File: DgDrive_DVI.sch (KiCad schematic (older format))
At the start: 26 parts, among them J1 Bias-T, J2 DVI-I, J3 Ld+, J4 Ld-, J5 Pz+, J6 Pz-, J7 Piezo_In, K1 G6AU, Q1 MMBT3904, Q2 2N4401

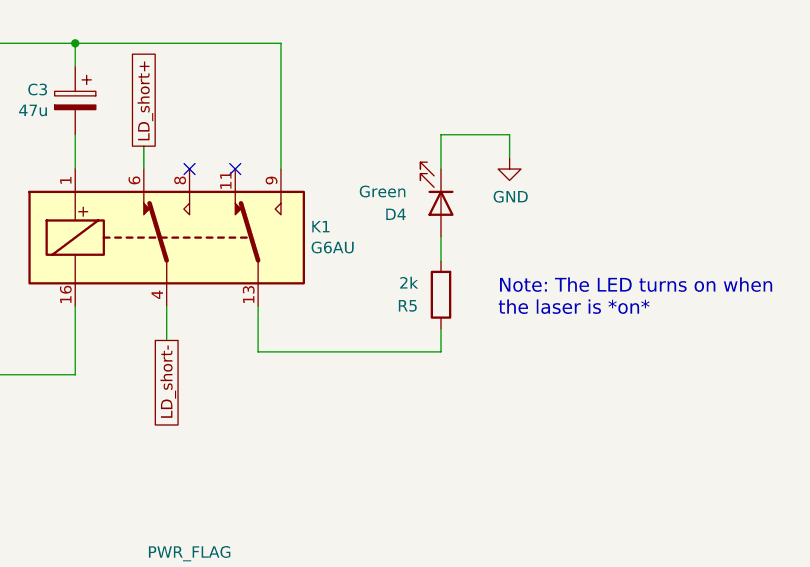
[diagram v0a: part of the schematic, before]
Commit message: Ld-: SMD Pad for shield
Fix footprints and replace Ld- THT with SMD pad
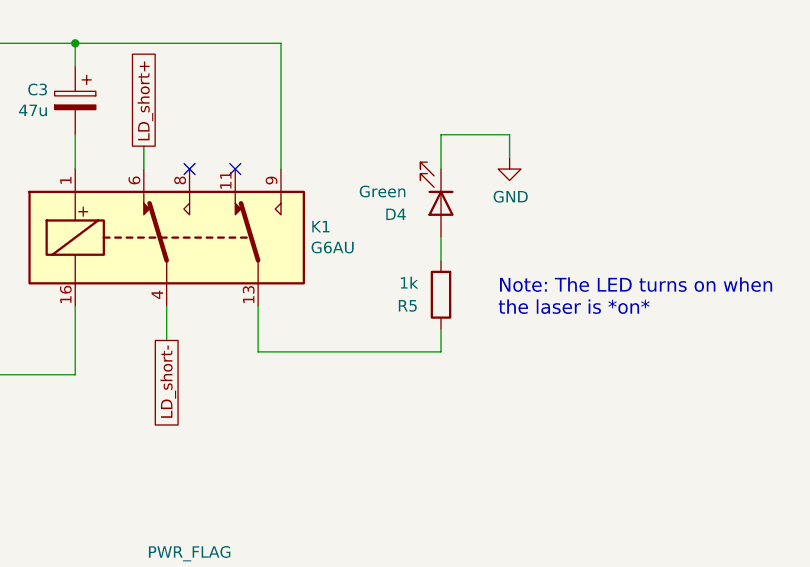
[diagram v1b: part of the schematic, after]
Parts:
- C3: footprint Capacitors_THT:CP_Radial_D5.0mm_P2.00mm -> Capacitor_THT:CP_Radial_D5.0mm_P2.00mm
- J3, J5, J6: footprint Wire_Pads:SolderWirePad_single_1mmDrill -> Connector_Wire:SolderWirePad_1x01_Drill1mm
- J4: footprint Wire_Pads:SolderWirePad_single_1mmDrill -> TestPoint:TestPoint_Keystone_5019_Minature
- R5: value 2k -> 1k; footprint Resistors_SMD:R_0603 -> Resistor_SMD:R_0603_1608Metric
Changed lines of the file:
@@
 Sheet 1 1
 Title "Laser Backplane Diode DVI"
-Date "2020-10-15"
-Rev "1.3"
+Date "2021-03-04"
+Rev "1.3.1"
 Comp "APQ"
 Comment1 "Tilman Preuschoff & Patrick Baus"
@@
 AR Path="/5BC1B30D" Ref="R5"  Part="1"
 F 0 "R5" H 6600 2100 50  0000 L CNN
-F 1 "2k" H 6600 2000 50  0000 L CNN
-F 2 "Resistors_SMD:R_0603" V 6430 2050 50  0001 C CNN
+F 1 "1k" H 6600 2000 50  0000 L CNN
+F 2 "Resistor_SMD:R_0603_1608Metric" V 6430 2050 50  0001 C CNN
 F 3 "~" H 6500 2050 50  0001 C CNN
 	1    6500 2050
@@
 F 0 "C3" H 5018 1246 50  0000 L CNN
 F 1 "47u" H 5018 1155 50  0000 L CNN
-F 2 "Capacitors_THT:CP_Radial_D5.0mm_P2.00mm" H 4938 1050 50  0001 C CNN
+F 2 "Capacitor_THT:CP_Radial_D5.0mm_P2.00mm" H 4938 1050 50  0001 C CNN
 F 3 "" H 4900 1200 50  0001 C CNN
 F 4 "Nichicon" H 4900 1200 60  0001 C CNN "MFN"
@@
 F 0 "J5" H 7568 4075 50  0000 C CNN
 F 1 "Pz+" H 7568 4166 50  0000 C CNN
-F 2 "Wire_Pads:SolderWirePad_single_1mmDrill" H 7650 4300 50  0001 C CNN
+F 2 "Connector_Wire:SolderWirePad_1x01_Drill1mm" H 7650 4300 50  0001 C CNN
 F 3 "~" H 7650 4300 50  0001 C CNN
 	1    7650 4300
@@
 F 0 "J6" H 7568 4425 50  0000 C CNN
 F 1 "Pz-" H 7568 4516 50  0000 C CNN
-F 2 "Wire_Pads:SolderWirePad_single_1mmDrill" H 7650 4650 50  0001 C CNN
+F 2 "Connector_Wire:SolderWirePad_1x01_Drill1mm" H 7650 4650 50  0001 C CNN
 F 3 "~" H 7650 4650 50  0001 C CNN
 	1    7650 4650
@@
 F 0 "J3" H 6930 5542 50  0000 L CNN
 F 1 "Ld+" H 6930 5451 50  0000 L CNN
-F 2 "Wire_Pads:SolderWirePad_single_1mmDrill" H 6850 5500 50  0001 C CNN
+F 2 "Connector_Wire:SolderWirePad_1x01_Drill1mm" H 6850 5500 50  0001 C CNN
 F 3 "~" H 6850 5500 50  0001 C CNN
 	1    6850 5500
@@
 F 0 "J4" H 6930 6142 50  0000 L CNN
 F 1 "Ld-" H 6930 6051 50  0000 L CNN
-F 2 "Wire_Pads:SolderWirePad_single_1mmDrill" H 6850 6100 50  0001 C CNN
+F 2 "TestPoint:TestPoint_Keystone_5019_Minature" H 6850 6100 50  0001 C CNN
 F 3 "~" H 6850 6100 50  0001 C CNN
 	1    6850 6100

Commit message: Incomplete: Add current source
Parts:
- removed C2: 3.3n (C0G), Capacitor_SMD:C_1206_3216Metric, symbol Device:C_Small
- removed R4: 49.9, Resistor_SMD:R_1210_3225Metric, symbol Device:R_Small
- removed TR1: SWB1010, Package_DIP:DIP-6_W7.62mm, symbol Transformer:ADT1-1
- added C? (x2): 10n, Capacitor_SMD:C_0603_1608Metric, symbol Device:C_Small
- added FB? (x2): BLM18KG102SZ1D, Inductor_SMD:L_0603_1608Metric, symbol Device:Ferrite_Bead_Small
- added L? (x2): 3.3u, custom:Coilcraft_XGL3530, symbol Device:L_Small
- added U?: LT1761-5, Package_TO_SOT_SMD:TSOT-23-5, symbol Regulator_Linear:LT1761-5
- J1: value Bias-T -> Curr. Mod.
- R1: value 5.6 / 750 mW -> 49.9; footprint Resistor_SMD:R_2512_6332Metric -> Resistor_SMD:R_0603_1608Metric; MFN Panasonic -> (none); MFP ERJ-1TRQF5R6U -> (none)
- R6: value 5.6 / 750 mW -> 49.9; footprint Resistor_SMD:R_2512_6332Metric -> Resistor_SMD:R_0603_1608Metric
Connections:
- net labels added: +12V, -12V, Curr_Mod
- net labels removed: Relay+
- wire segments 89 -> 100
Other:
- moved on the sheet: J1, J3, J4, J5, J6, J7, Q2, R1, R2, R6, R7, R8

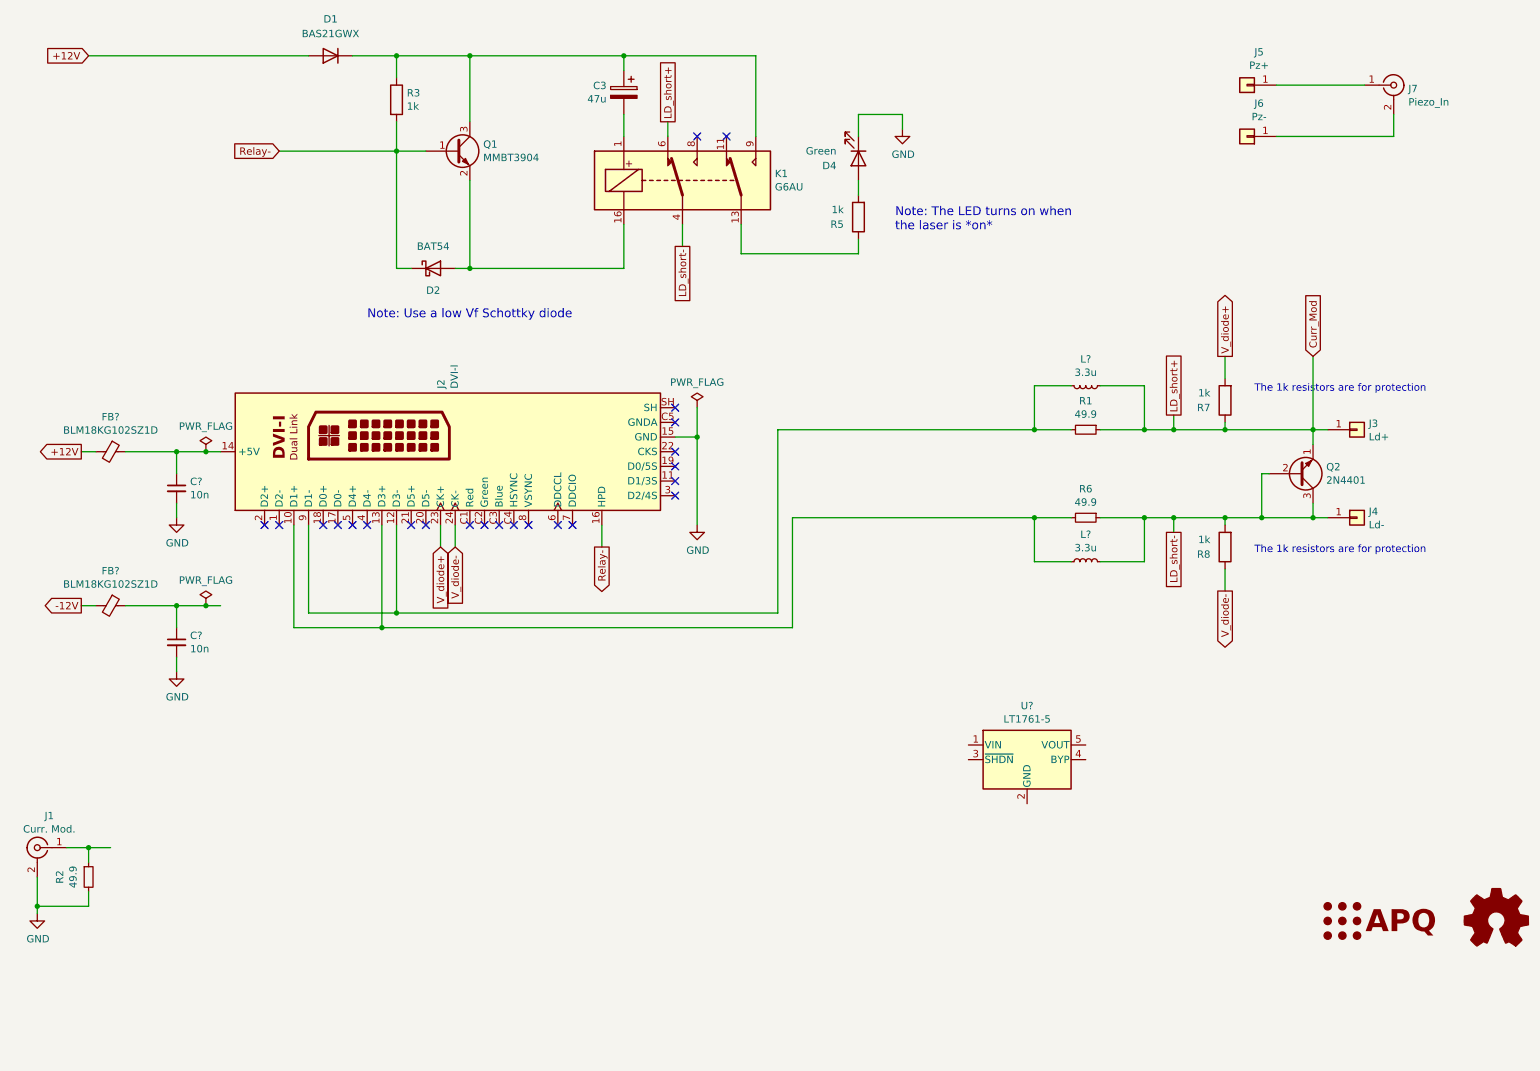
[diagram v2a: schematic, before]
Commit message: Add current source
Replace Bias-T with Howland current source. The current source requires additional negative supply (Pin7).

Replace large resistors with inductors+49.9-resistors.
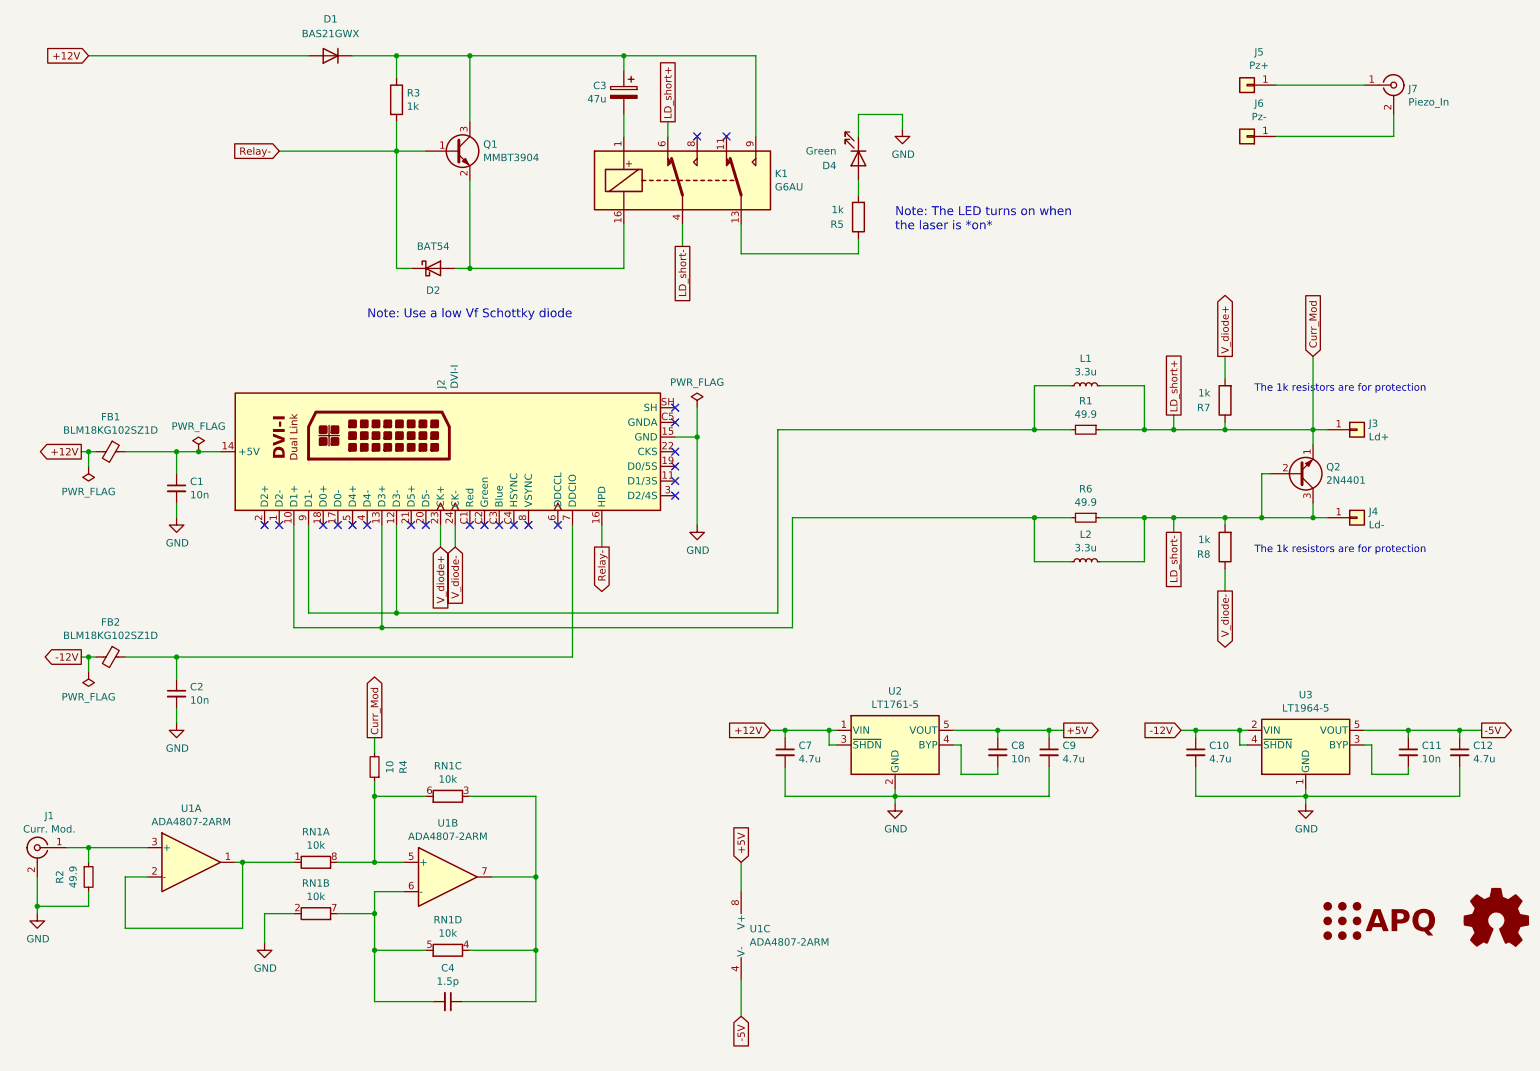
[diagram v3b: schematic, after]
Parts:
- added C10, C12, C7, C9: 4.7u, Capacitor_SMD:C_0805_2012Metric, symbol Device:C_Small
- added C11, C8: 10n, Capacitor_SMD:C_0603_1608Metric, symbol Device:C_Small
- added C4: 1.5p, Capacitor_SMD:C_0603_1608Metric, symbol Device:C_Small
- added R4: 10, Resistor_SMD:R_0603_1608Metric, symbol Device:R_Small
- added RN1: 10k, custom:MSOP-8_3x3mm_P0.65mm_mod, symbol Device:R_Pack04_Split
- added U1: ADA4807-2ARM, custom:MSOP-8_3x3mm_P0.65mm_mod, symbol Amplifier_Operational:ADA4807-2ARM
- added U3: LT1964-5, Package_TO_SOT_SMD:TSOT-23-5, symbol Regulator_Linear:LT1964-5
- R6: MFN Panasonic -> (none); MFP ERJ-1TRQF5R6U -> (none)
- gave numbers to parts that had none: 7
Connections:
- net +12V: now also U2.1 (VIN), U2.3 (~SHDN), C7.1
- net -12V: now also C10.1, U3.2 (VIN), U3.4 (~SHDN)
- net Curr_Mod: now also L1.2, R4.2; no longer L1.1
- net GND: now also U2.2 (GND), C10.2, C12.2, C7.2, C9.2, RN1.2 (R2.1), U3.1 (GND)
- net at J1.1 (In), R2.1: now also U1.3 (+)
- net at J2.12 (D3-), J2.9 (D1-), R1.2: now also L1.1; no longer L1.2
- net at J2.7 (DDCIO): now also C2.1, FB2.1
- net at U2.4 (BYP): now also C8.2
- net +5V: now reaches U2.5 (VOUT)
- net +5V: now also C8.1, C9.1, U1.8 (V+)
- new net: C11.2, U3.3 (BYP)
- new net: RN1.1 (R1.1), U1.1, U1.2 (-)
- new net: R4.1, RN1.6 (R3.2), RN1.8 (R1.2), U1.5 (+)
- new net: C4.2, RN1.5 (R4.2), RN1.7 (R2.2), U1.6 (-)
- new net: C4.1, RN1.3 (R3.1), RN1.4 (R4.1), U1.7
- new net -5V: C11.1, C12.1, U1.4 (V-), U3.5 (VOUT)
- no-connect marks 23 -> 22
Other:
- moved on the sheet: C2, FB2, L1, U2

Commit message: Updated Gerber files to 1.4 Added EEPROM
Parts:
- added U4: AT21CS11-STXXXX-X, Package_TO_SOT_SMD:SOT-23, symbol Microchip:AT21CS11-STXXXX-X
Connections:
- net GND: now also U4.3 (GND)
- net at J2.6 (DDCCL): now also C2.1, FB2.1
- new net: J2.7 (DDCIO), U4.1 (SI/O)
- no-connect marks 22 -> 21
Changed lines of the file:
@@
 NoConn ~ 4150 4150
 NoConn ~ 4250 4150
-NoConn ~ 4450 4150
 Text GLabel 1200 3650 0    50   Output ~ 0
 +12V
@@
 	8700 5550 8800 5550
 Connection ~ 8800 5550
-$Comp
-L Regulator_Linear:LT1964-5 U3
-U 1 1 6052EB9E
-P 9550 5650
-F 0 "U3" H 9550 5308 50  0000 C CNN
-F 1 "LT1964-5" H 9550 5399 50  0000 C CNN
-F 2 "Package_TO_SOT_SMD:TSOT-23-5" H 9550 5350 50  0001 C CNN
-F 3 "https://www.analog.com/media/en/technical-documentation/data-sheets/1964fb.pdf" H 9550 5650 50  0001 C CNN
-	1    9550 5650
-	1    0    0    1
-$EndComp
 Text GLabel 7900 5550 2    50   Output ~ 0
 +5V
@@
 Text GLabel 5700 7500 3    50   Input ~ 0
 -5V
-Wire Wire Line
-	4550 4150 4550 5050
 $Comp
 L Device:R_Small R4
@@
 	1250 5150 1250 5050
 Wire Wire Line
-	1850 5050 4550 5050
+	1850 5050 4450 5050
 Connection ~ 1250 5050
 Wire Wire Line
@@
 Wire Wire Line
 	5700 7250 5700 7500
+Wire Wire Line
+	4450 4150 4450 5050
+$Comp
+L Microchip:AT21CS11-STXXXX-X U4
+U 1 1 60A01FFA
+P 6850 4550
+F 0 "U4" H 6500 4550 50  0000 R CNN
+F 1 "AT21CS11-STXXXX-X" H 6500 4450 50  0000 R CNN
+F 2 "Package_TO_SOT_SMD:SOT-23" H 6850 4550 50  0001 C CNN
+F 3 "https://ww1.microchip.com/downloads/en/DeviceDoc/AT21CS01-AT21CS11-Data-Sheet-DS20005857D.pdf" H 6850 4550 50  0001 C CNN
+	1    6850 4550
+	-1   0    0    -1
+$EndComp
+$Comp
+L power:GND #PWR0109
+U 1 1 60A12DE2
+P 6850 4950
+F 0 "#PWR0109" H 6850 4700 50  0001 C CNN
+F 1 "GND" H 6855 4777 50  0000 C CNN
+F 2 "" H 6850 4950 50  0001 C CNN
+F 3 "" H 6850 4950 50  0001 C CNN
+	1    6850 4950
+	1    0    0    -1
+$EndComp
+Wire Wire Line
+	6850 4950 6850 4850
+Wire Wire Line
+	4550 4150 4550 4650
+Wire Wire Line
+	4550 4650 6150 4650
+Wire Wire Line
+	6150 4650 6150 4550
+Wire Wire Line
+	6150 4550 6450 4550
+$Comp
+L Regulator_Linear:LT1964-5 U3
+U 1 1 6052EB9E
+P 9550 5650
+F 0 "U3" H 9550 5308 50  0000 C CNN
+F 1 "LT1964-5" H 9550 5399 50  0000 C CNN
+F 2 "Package_TO_SOT_SMD:TSOT-23-5" H 9550 5350 50  0001 C CNN
+F 3 "https://www.analog.com/media/en/technical-documentation/data-sheets/1964fb.pdf" H 9550 5650 50  0001 C CNN
+	1    9550 5650
+	1    0    0    1
+$EndComp
 $EndSCHEMATC

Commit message: Update BOM
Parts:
- C11, C8: MFN (none) -> Murata Electronics; PN (none) -> GRM1885C1H103JA01J
- J1, J3, J4, J5, J6, J7, LOGO1, LOGO2, U4: Config (none) -> DNF
- J2: MFP CDVI-F29VDG1-P1 -> (none); PN (none) -> CDVI-F29VDG1-P1
- L1, L2: PN XGL3530-332ME_ -> XGL3530-332MEC
- Q1: MFN (none) -> Nexperia; PN (none) -> MMBT3904VL
- Q2: MPN 2N4401BU -> (none); PN (none) -> 2N4401BU
- R2: MFN (none) -> Yageo; PN (none) -> RC1210FR-0749R9L
- R5: MFN (none) -> Susumu; PN (none) -> RR0816P-102-D
- U1: MFN (none) -> Analog Devices; PN (none) -> ADA4807-2ARMZ
- U2: MFN (none) -> Linear Technology; PN (none) -> LT1761ES5-5#TRPBF
- U3: MFN (none) -> Linear Technology; PN (none) -> LT1964ES5-5#TRPBF
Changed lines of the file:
@@
 F 2 "Resistor_SMD:R_0603_1608Metric" V 6430 2050 50  0001 C CNN
 F 3 "~" H 6500 2050 50  0001 C CNN
+F 4 "Susumu" H 6500 2050 50  0001 C CNN "MFN"
+F 5 "RR0816P-102-D" H 6500 2050 50  0001 C CNN "PN"
 	1    6500 2050
 	-1   0    0    1
@@
 F 3 "" H 3275 3650 50  0001 C CNN
 F 4 "Conn_Link" H 3250 3650 50  0001 C CNN "MFN"
-F 5 "CDVI-F29VDG1-P1" H 3250 3650 50  0001 C CNN "MFP"
+F 5 "CDVI-F29VDG1-P1" H 3250 3650 50  0001 C CNN "PN"
 	1    3250 3650
 	0    -1   -1   0
@@
 F 2 "Connector_Coaxial:SMA_Amphenol_901-144_Vertical" H 900 6350 50  0001 C CNN
 F 3 "~" H 900 6350 50  0001 C CNN
+F 4 "DNF" H 900 6350 50  0001 C CNN "Config"
 	1    900  6350
 	-1   0    0    -1
@@
 F 2 "Resistor_SMD:R_1210_3225Metric" H 1250 6550 50  0001 C CNN
 F 3 "~" H 1250 6550 50  0001 C CNN
+F 4 "Yageo" V 1250 6550 50  0001 C CNN "MFN"
+F 5 "RC1210FR-0749R9L" V 1250 6550 50  0001 C CNN "PN"
 	1    1250 6550
 	1    0    0    -1
@@
 F 2 "Package_TO_SOT_SMD:SOT-23" H 3950 1525 50  0001 L CIN
 F 3 "https://www.fairchildsemi.com/datasheets/2N/2N3904.pdf" H 3750 1600 50  0001 L CNN
+F 4 "Nexperia" H 3750 1600 50  0001 C CNN "MFN"
+F 5 "MMBT3904VL" H 3750 1600 50  0001 C CNN "PN"
 	1    3750 1600
 	1    0    0    -1
@@
 F 2 "Connector_Coaxial:SMA_Amphenol_901-144_Vertical" H 10150 1150 50  0001 C CNN
 F 3 " ~" H 10150 1150 50  0001 C CNN
+F 4 "DNF" H 10150 1150 50  0001 C CNN "Config"
 	1    10150 1150
 	1    0    0    -1
@@
 F 2 "Connector_Wire:SolderWirePad_1x01_Drill1mm" H 9150 1150 50  0001 C CNN
 F 3 "~" H 9150 1150 50  0001 C CNN
+F 4 "DNF" H 9150 1150 50  0001 C CNN "Config"
 	1    9150 1150
 	-1   0    0    1
@@
 F 2 "Connector_Wire:SolderWirePad_1x01_Drill1mm" H 9150 1500 50  0001 C CNN
 F 3 "~" H 9150 1500 50  0001 C CNN
+F 4 "DNF" H 9150 1500 50  0001 C CNN "Config"
 	1    9150 1500
 	-1   0    0    1
@@
 F 2 "Connector_Wire:SolderWirePad_1x01_Drill1mm" H 9900 3500 50  0001 C CNN
 F 3 "~" H 9900 3500 50  0001 C CNN
+F 4 "DNF" H 9900 3500 50  0001 C CNN "Config"
 	1    9900 3500
 	1    0    0    -1
@@
 F 2 "TestPoint:TestPoint_Keystone_5019_Minature" H 9900 4100 50  0001 C CNN
 F 3 "~" H 9900 4100 50  0001 C CNN
+F 4 "DNF" H 9900 4100 50  0001 C CNN "Config"
 	1    9900 4100
 	1    0    0    -1
@@
 F 3 "~" H 9500 3800 50  0001 C CNN
 F 4 "ON Semiconductor" H 9500 3800 50  0001 C CNN "MFN"
-F 5 "2N4401BU" H 9500 3800 50  0001 C CNN "MPN"
+F 5 "2N4401BU" H 9500 3800 50  0001 C CNN "PN"
 	1    9500 3800
 	1    0    0    1
@@
 F 2 "Symbol:OSHW-Logo_7.5x8mm_SilkScreen" H 10850 6850 50  0001 C CNN
 F 3 "~" H 10850 6850 50  0001 C CNN
+F 4 "DNF" H 10850 6850 50  0001 C CNN "Config"
 	1    10850 6850
 	1    0    0    -1
@@
 F 2 "custom:APQ-Logo_small" H 9800 6850 50  0001 C CNN
 F 3 "~" H 9800 6850 50  0001 C CNN
+F 4 "DNF" H 9500 6850 50  0001 C CNN "Config"
 	1    9500 6850
 	1    0    0    -1
@@
 F 3 "~" H 8050 3200 50  0001 C CNN
 F 4 "Coilcraft" V 8050 3200 50  0001 C CNN "MFN"
-F 5 "XGL3530-332ME_ " V 8050 3200 50  0001 C CNN "PN"
+F 5 "XGL3530-332MEC" V 8050 3200 50  0001 C CNN "PN"
 	1    8050 3200
 	0    -1   -1   0
@@
 F 3 "~" H 8050 4400 50  0001 C CNN
 F 4 "Coilcraft" V 8050 4400 50  0001 C CNN "MFN"
-F 5 "XGL3530-332ME_ " V 8050 4400 50  0001 C CNN "PN"
+F 5 "XGL3530-332MEC" V 8050 4400 50  0001 C CNN "PN"
 	1    8050 4400
 	0    -1   -1   0
@@
 F 2 "Package_TO_SOT_SMD:TSOT-23-5" H 6750 5975 50  0001 C CNN
 F 3 "https://www.analog.com/media/en/technical-documentation/data-sheets/1761sff.pdf" H 6750 5650 50  0001 C CNN
+F 4 "Linear Technology" H 6750 5650 50  0001 C CNN "MFN"
+F 5 "LT1761ES5-5#TRPBF" H 6750 5650 50  0001 C CNN "PN"
 	1    6750 5650
 	1    0    0    -1
@@
 F 2 "Capacitor_SMD:C_0603_1608Metric" H 7450 5700 50  0001 C CNN
 F 3 "~" H 7450 5700 50  0001 C CNN
+F 4 "Murata Electronics" H 7450 5700 50  0001 C CNN "MFN"
+F 5 "GRM1885C1H103JA01J" H 7450 5700 50  0001 C CNN "PN"
 	1    7450 5700
 	1    0    0    -1
@@
 F 2 "Capacitor_SMD:C_0603_1608Metric" H 10250 5700 50  0001 C CNN
 F 3 "~" H 10250 5700 50  0001 C CNN
+F 4 "Murata Electronics" H 10250 5700 50  0001 C CNN "MFN"
+F 5 "GRM1885C1H103JA01J" H 10250 5700 50  0001 C CNN "PN"
 	1    10250 5700
 	1    0    0    -1
@@
 F 2 "custom:MSOP-8_3x3mm_P0.65mm_mod" H 1950 6450 50  0001 C CNN
 F 3 "https://www.analog.com/media/en/technical-documentation/data-sheets/ADA4807-1_4807-2_4807-4.pdf" H 1950 6450 50  0001 C CNN
+F 4 "Analog Devices" H 1950 6450 50  0001 C CNN "MFN"
+F 5 "ADA4807-2ARMZ" H 1950 6450 50  0001 C CNN "PN"
 	1    1950 6450
 	1    0    0    -1
@@
 F 2 "custom:MSOP-8_3x3mm_P0.65mm_mod" H 3700 6550 50  0001 C CNN
 F 3 "https://www.analog.com/media/en/technical-documentation/data-sheets/ADA4807-1_4807-2_4807-4.pdf" H 3700 6550 50  0001 C CNN
+F 4 "Analog Devices" H 3700 6550 50  0001 C CNN "MFN"
+F 5 "ADA4807-2ARMZ" H 3700 6550 50  0001 C CNN "PN"
 	2    3700 6550
 	1    0    0    -1
@@
 F 2 "Package_TO_SOT_SMD:SOT-23" H 6850 4550 50  0001 C CNN
 F 3 "https://ww1.microchip.com/downloads/en/DeviceDoc/AT21CS01-AT21CS11-Data-Sheet-DS20005857D.pdf" H 6850 4550 50  0001 C CNN
+F 4 "DNF" H 6850 4550 50  0001 C CNN "Config"
 	1    6850 4550
 	-1   0    0    -1
@@
 F 2 "Package_TO_SOT_SMD:TSOT-23-5" H 9550 5350 50  0001 C CNN
 F 3 "https://www.analog.com/media/en/technical-documentation/data-sheets/1964fb.pdf" H 9550 5650 50  0001 C CNN
+F 4 "Linear Technology" H 9550 5650 50  0001 C CNN "MFN"
+F 5 "LT1964ES5-5#TRPBF" H 9550 5650 50  0001 C CNN "PN"
 	1    9550 5650
 	1    0    0    1
